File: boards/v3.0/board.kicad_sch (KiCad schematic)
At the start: 65 parts, among them J2 KF301-2P, J3 KF301-2P, J4 KF301-2P, J5 KF301-2P, J6 KF301-2P, J7 KF301-2P, P1 Pin Header, P2 Pin Header, P3 Pin Header, P4 Pin Header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

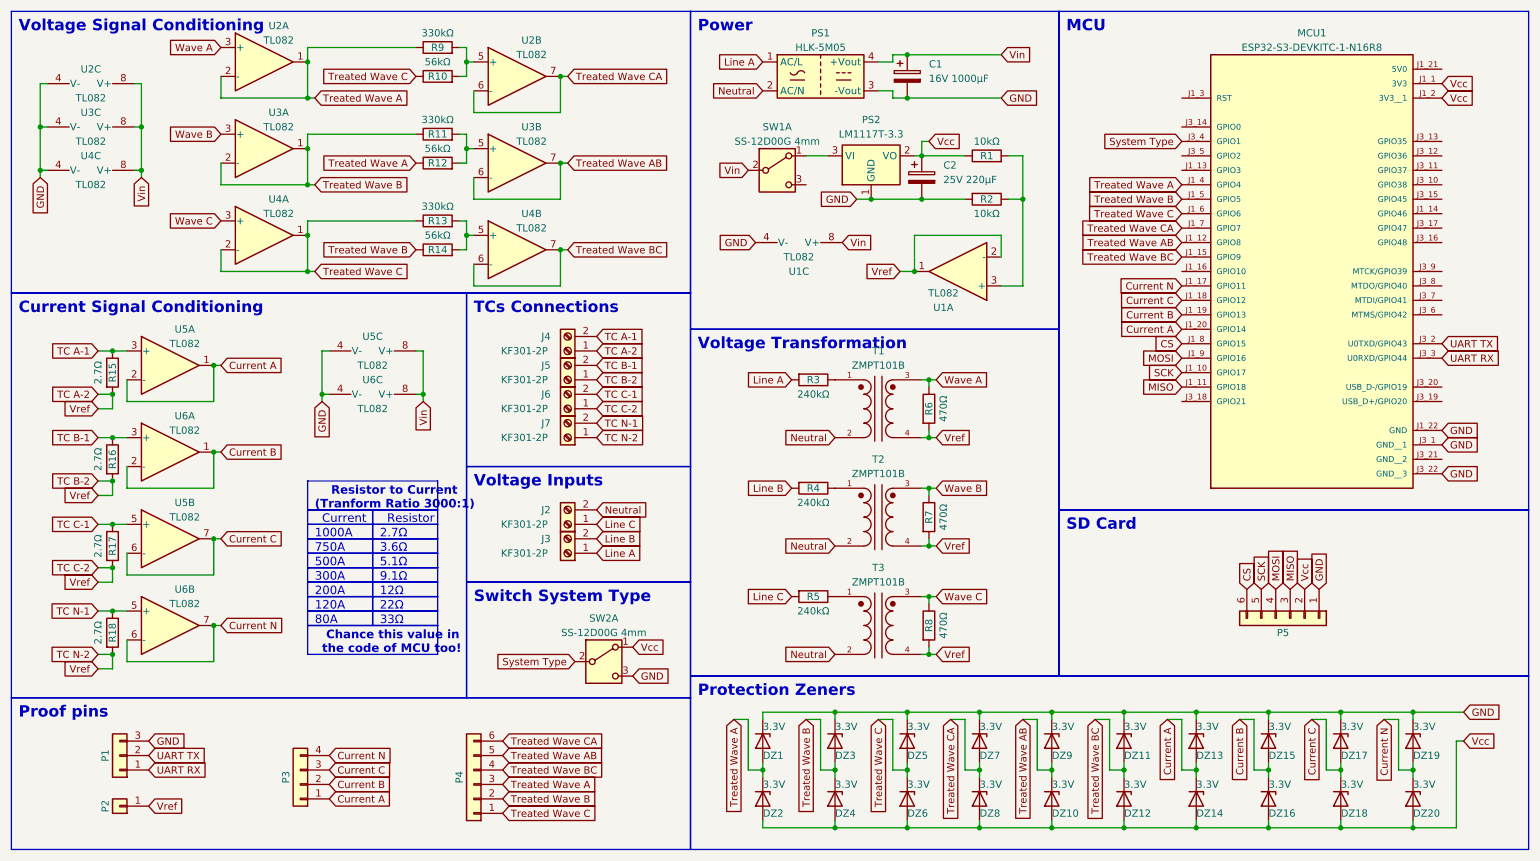
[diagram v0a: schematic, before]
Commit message: Finish of board v3.0 development and code update
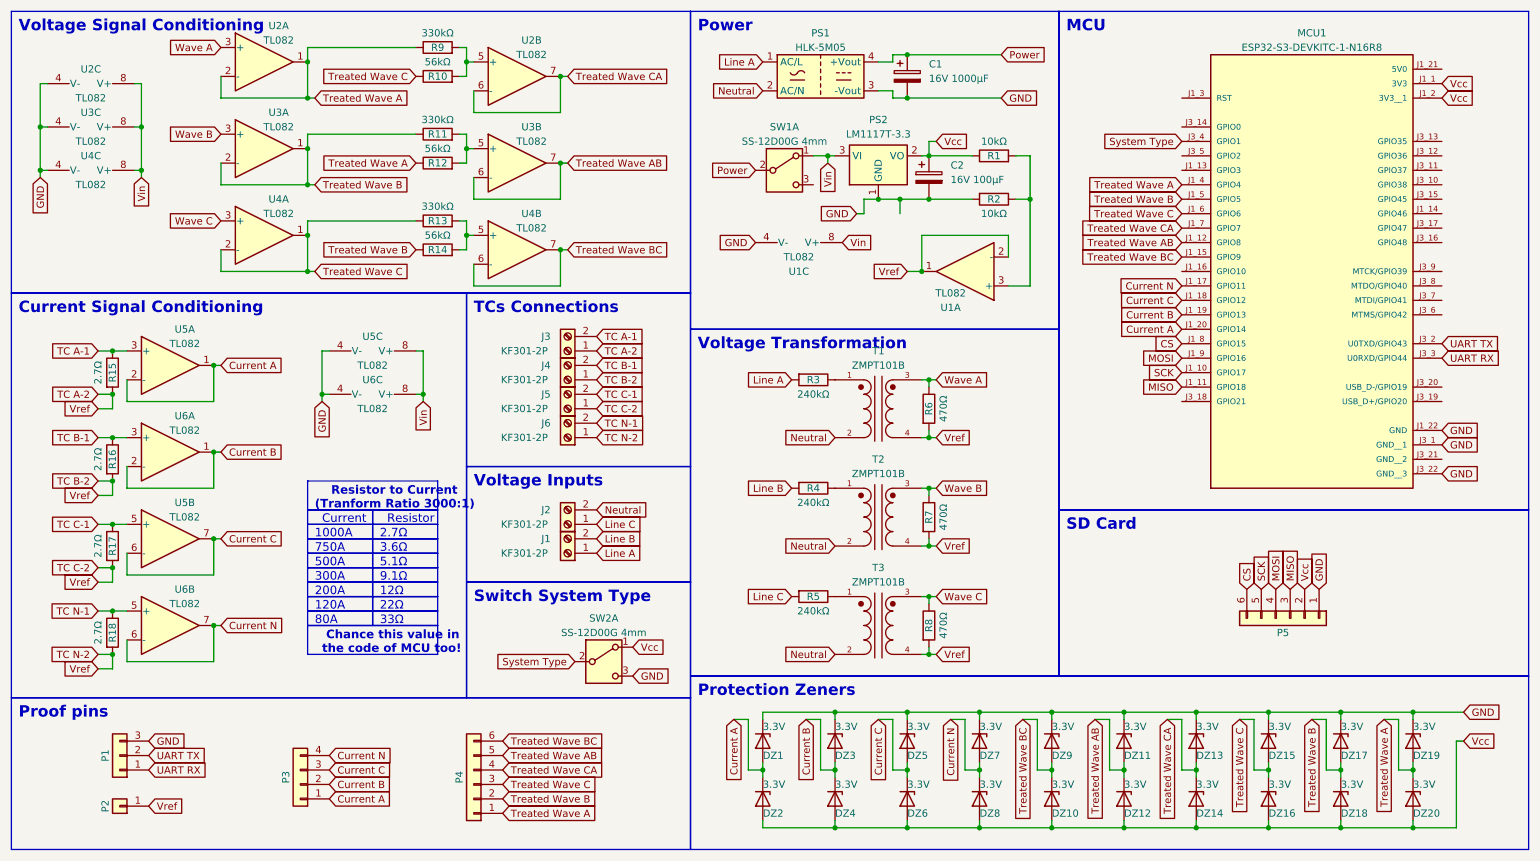
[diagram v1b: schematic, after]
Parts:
- C2: value 25V 220µF -> 16V 100µF; footprint Capacitor_THT:CP_Radial_D6.3mm_P2.50mm -> Capacitor_THT:CP_Radial_D5.0mm_P2.00mm
- renumbered J3 to J1, J4 to J3, J5 to J4, J6 to J5, J7 to J6
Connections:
- net Current A: now also DZ1.2 (A), DZ2.1 (K); no longer DZ13.2 (A), DZ14.1 (K)
- net Current B: now also DZ3.2 (A), DZ4.1 (K); no longer DZ15.2 (A), DZ16.1 (K)
- net Current C: now also DZ5.2 (A), DZ6.1 (K); no longer DZ17.2 (A), DZ18.1 (K)
- net Current N: now also DZ7.2 (A), DZ8.1 (K); no longer DZ19.2 (A), DZ20.1 (K)
- net Treated Wave A: now also DZ19.2 (A), DZ20.1 (K), P4.1 (Pin_1); no longer DZ1.2 (A), DZ2.1 (K), P4.3 (Pin_3)
- net Treated Wave AB: now also DZ11.2 (A), DZ12.1 (K); no longer DZ10.1 (K), DZ9.2 (A)
- net Treated Wave B: now also DZ17.2 (A), DZ18.1 (K); no longer DZ3.2 (A), DZ4.1 (K)
- net Treated Wave BC: now also DZ10.1 (K), DZ9.2 (A), P4.6 (Pin_6); no longer DZ11.2 (A), DZ12.1 (K), P4.4 (Pin_4)
- net Treated Wave C: now also DZ15.2 (A), DZ16.1 (K), P4.3 (Pin_3); no longer DZ5.2 (A), DZ6.1 (K), P4.1 (Pin_1)
- net Treated Wave CA: now also DZ13.2 (A), DZ14.1 (K), P4.4 (Pin_4); no longer DZ7.2 (A), DZ8.1 (K), P4.6 (Pin_6)
- net Vin: now also PS2.3 (VI), SW1.1 (A); no longer C1.1, PS1.4 (+Vout), SW1.2 (B)
- new net Power: C1.1, PS1.4 (+Vout), SW1.2 (B)
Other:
- moved on the sheet: C2, PS2, R1, R2, SW1A, U1A

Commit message: Revision of the v3.0 board
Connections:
- net Current A: now also U6.1, U6.2 (-); no longer U5.1, U5.2 (-)
- net Current B: now also U5.1, U5.2 (-); no longer U6.1, U6.2 (-)
- net TC A-1: now also R17.1, U6.3 (+); no longer R15.1, U5.3 (+)
- net TC B-1: now also R15.1, U5.3 (+); no longer R16.1, U6.3 (+)
- net TC C-1: now also R16.1; no longer R17.1

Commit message: Reduction in the size of v3.0 board
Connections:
- net Vcc: no longer MCU1.J1_2 (3V3__1)
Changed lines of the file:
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@@
   (title_block
     (title "ESP32 Power Analyser V3.0 Schematics")
-    (date "03/05/2024")
-    (rev "1.3")
+    (date "04/05/2024")
+    (rev "1.4")
     (company "https://www.linkedin.com/in/lucasrguerra")
   )
@@
       (effects (font (size 1.27 1.27)) (justify left) hide)
     )
-  )
-  (global_label "Vcc" (shape input) (at 266.7 30.48 0) (fields_autoplaced)
-    (effects (font (size 1.27 1.27)) (justify left))
-    (property "Intersheetrefs" "${INTERSHEET_REFS}" (at 272.951 30.48 0)
-      (effects (font (size 1.27 1.27)) (justify left) hide)
-    )

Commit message: Revision in the v3.0 board
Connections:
- net Treated Wave AB: now also MCU1.J1_7 (GPIO7); no longer MCU1.J1_12 (GPIO8)
- net Treated Wave B: now also MCU1.J1_6 (GPIO6); no longer MCU1.J1_5 (GPIO5)
- net Treated Wave C: now also MCU1.J1_12 (GPIO8); no longer MCU1.J1_6 (GPIO6)
- net Treated Wave CA: now also MCU1.J1_5 (GPIO5); no longer MCU1.J1_7 (GPIO7)
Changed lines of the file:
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@@
     (title "ESP32 Power Analyser V3.0 Schematics")
     (date "04/05/2024")
-    (rev "1.4")
+    (rev "1.5")
     (company "https://www.linkedin.com/in/lucasrguerra")
   )
@@
     )
   )
+  (global_label "Treated Wave CA" (shape input) (at 220.98 48.26 180) (fields_autoplaced)
+    (effects (font (size 1.27 1.27)) (justify right))
+    (property "Intersheetrefs" "${INTERSHEET_REFS}" (at 202.0897 48.26 0)
+      (effects (font (size 1.27 1.27)) (justify right) hide)
+    )
+  )
   (global_label "Vcc" (shape input) (at 124.46 127 0) (fields_autoplaced)
     (effects (font (size 1.27 1.27)) (justify left))
@@
     )
   )
-  (global_label "Treated Wave AB" (shape input) (at 220.98 55.88 180) (fields_autoplaced)
-    (effects (font (size 1.27 1.27)) (justify right))
-    (property "Intersheetrefs" "${INTERSHEET_REFS}" (at 202.0897 55.88 0)
-      (effects (font (size 1.27 1.27)) (justify right) hide)
-    )
-  )
   (global_label "Neutral" (shape input) (at 118.11 102.87 0) (fields_autoplaced)
     (effects (font (size 1.27 1.27)) (justify left))
@@
     )
   )
+  (global_label "Treated Wave C" (shape input) (at 220.98 55.88 180) (fields_autoplaced)
+    (effects (font (size 1.27 1.27)) (justify right))
+    (property "Intersheetrefs" "${INTERSHEET_REFS}" (at 203.1783 55.88 0)
+      (effects (font (size 1.27 1.27)) (justify right) hide)
+    )
+  )
   (global_label "Vref" (shape input) (at 30.48 100.33 180) (fields_autoplaced)
     (effects (font (size 1.27 1.27)) (justify right))
@@
     )
   )
+  (global_label "Treated Wave B" (shape input) (at 220.98 50.8 180) (fields_autoplaced)
+    (effects (font (size 1.27 1.27)) (justify right))
+    (property "Intersheetrefs" "${INTERSHEET_REFS}" (at 203.1783 50.8 0)
+      (effects (font (size 1.27 1.27)) (justify right) hide)
+    )
+  )
   (global_label "Neutral" (shape input) (at 160.02 90.17 180) (fields_autoplaced)
     (effects (font (size 1.27 1.27)) (justify right))
@@
     )
   )
+  (global_label "Treated Wave AB" (shape input) (at 220.98 53.34 180) (fields_autoplaced)
+    (effects (font (size 1.27 1.27)) (justify right))
+    (property "Intersheetrefs" "${INTERSHEET_REFS}" (at 202.0897 53.34 0)
+      (effects (font (size 1.27 1.27)) (justify right) hide)
+    )
+  )
   (global_label "Treated Wave B" (shape input) (at 101.6 153.67 0) (fields_autoplaced)
     (effects (font (size 1.27 1.27)) (justify left))
@@
     )
   )
-  (global_label "Treated Wave B" (shape input) (at 220.98 48.26 180) (fields_autoplaced)
-    (effects (font (size 1.27 1.27)) (justify right))
-    (property "Intersheetrefs" "${INTERSHEET_REFS}" (at 203.1783 48.26 0)
-      (effects (font (size 1.27 1.27)) (justify right) hide)
-    )
-  )
   (global_label "Vcc" (shape input) (at 266.7 27.94 0) (fields_autoplaced)
     (effects (font (size 1.27 1.27)) (justify left))
@@
     )
   )
-  (global_label "Treated Wave CA" (shape input) (at 220.98 53.34 180) (fields_autoplaced)
-    (effects (font (size 1.27 1.27)) (justify right))
-    (property "Intersheetrefs" "${INTERSHEET_REFS}" (at 202.0897 53.34 0)
-      (effects (font (size 1.27 1.27)) (justify right) hide)
-    )
-  )
   (global_label "Wave B" (shape input) (at 177.8 99.06 0) (fields_autoplaced)
     (effects (font (size 1.27 1.27)) (justify left))
@@
       (effects (font (size 1.27 1.27)) (justify right) hide)
     )
-  )
-  (global_label "Treated Wave C" (shape input) (at 220.98 50.8 180) (fields_autoplaced)
-    (effects (font (size 1.27 1.27)) (justify right))
-    (property "Intersheetrefs" "${INTERSHEET_REFS}" (at 203.1783 50.8 0)
-      (effects (font (size 1.27 1.27)) (justify right) hide)
-    )
